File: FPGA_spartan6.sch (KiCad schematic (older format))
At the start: 46 parts, among them J6 Conn_02x10_Odd_Even, U10 lx9_XC6SLX9-TQ144, U11 FSM1LPTR, U12 FSM1LPTR, U13 FSM1LPTR, U9 CY7C199, X1 Oscillator_ASE-xxxMHz

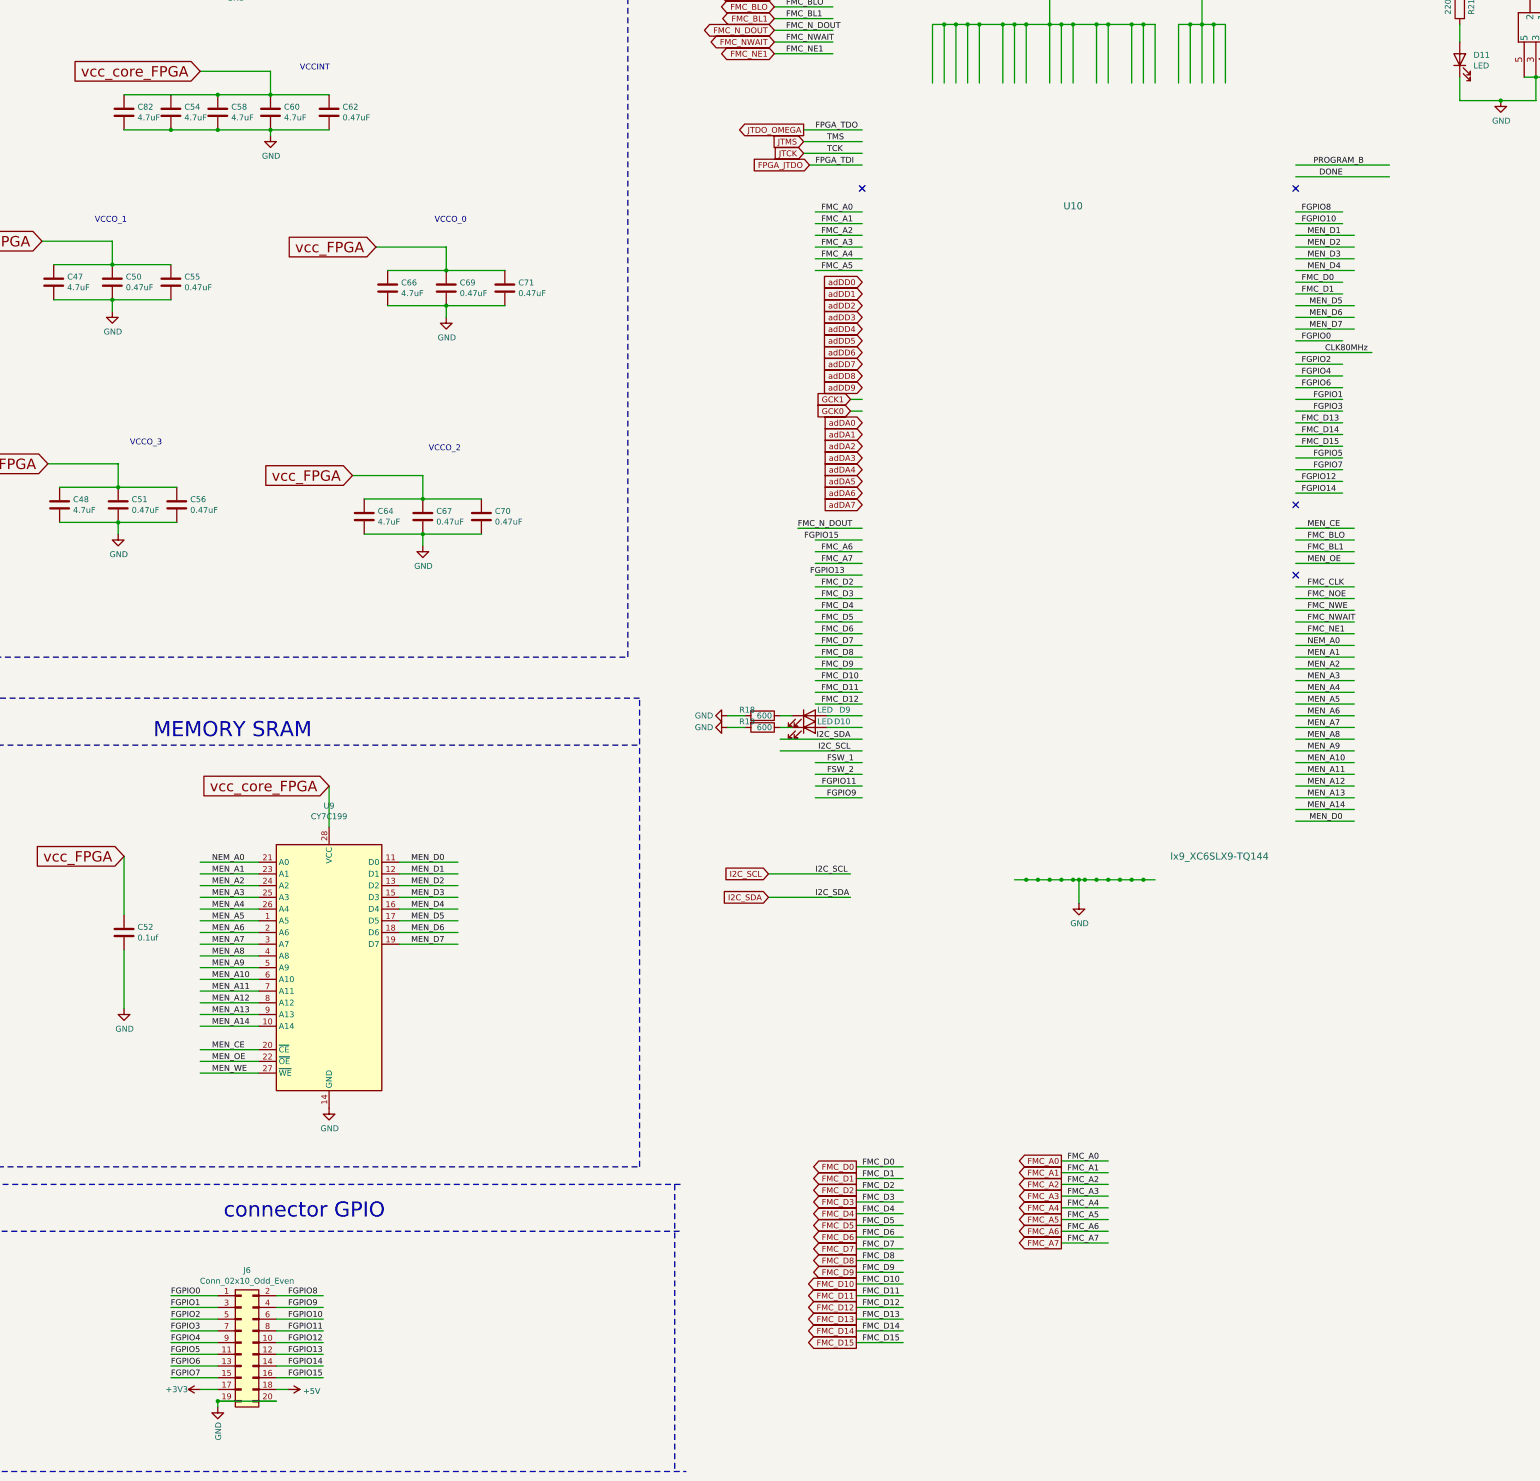
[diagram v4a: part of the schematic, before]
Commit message: diseño de esquematico fm
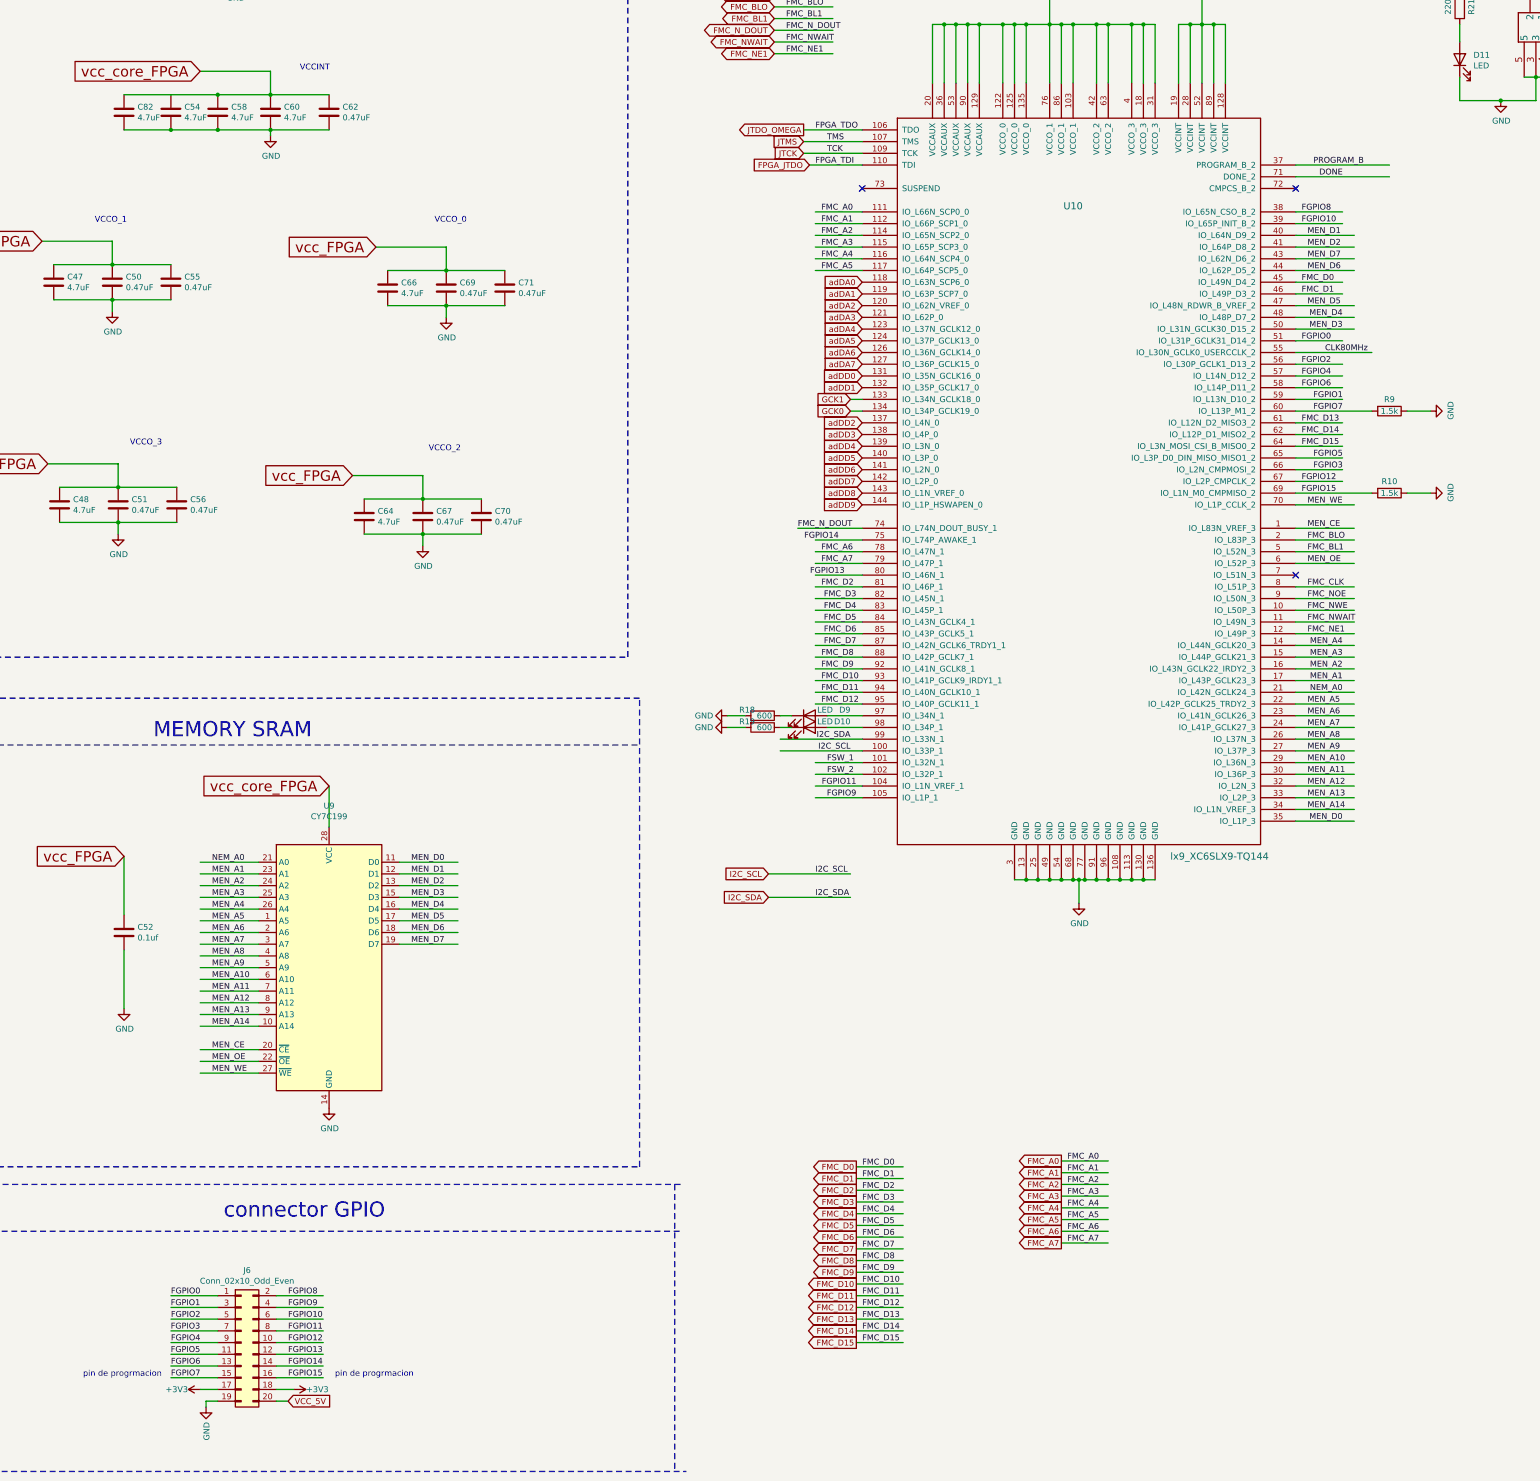
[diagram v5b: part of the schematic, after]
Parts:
- added R10, R9: 1.5k, Resistor_SMD:R_0603_1608Metric_Pad1.05x0.95mm_HandSolder, symbol BAT2032:R
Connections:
- net labels added: VCC_5V
- net labels removed: +5V
- wire segments 342 -> 346
- no-connect marks 4 -> 3
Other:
- note added: "pin de progrmacion\n"
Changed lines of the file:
@@
 	7700 13150 1200 13150
 Wire Wire Line
-	12950 5150 13450 5150
+	12950 5650 13450 5650
+Wire Wire Line
+	12950 5350 13450 5350
 Wire Wire Line
 	12950 5250 13450 5250
-Wire Wire Line
-	12950 5350 13450 5350
-Wire Wire Line
-	13450 5650 12950 5650
-Wire Wire Line
-	13450 5750 12950 5750
-Wire Wire Line
-	13450 5850 12950 5850
-Text Label 13050 5150 0    50   ~ 0
-MEN_D2
+Text Label 13050 5650 0    50   ~ 0
+MEN_D5
+Text Label 13050 5350 0    50   ~ 0
+MEN_D6
 Text Label 13050 5250 0    50   ~ 0
-MEN_D3
-Text Label 13050 5350 0    50   ~ 0
-MEN_D4
-Text Label 13350 5650 2    50   ~ 0
-MEN_D5
-Text Label 13350 5750 2    50   ~ 0
-MEN_D6
-Text Label 13350 5850 2    50   ~ 0
 MEN_D7
-Text Label 13050 5050 0    50   ~ 0
-MEN_D1
 Text Label 13350 10050 2    50   ~ 0
 MEN_D0
 Wire Wire Line
-	12950 5050 13450 5050
-Wire Wire Line
 	13450 10050 12950 10050
 Wire Wire Line
-	13450 8550 12950 8550
-Wire Wire Line
-	13450 8650 12950 8650
-Wire Wire Line
-	13450 8750 12950 8750
-Wire Wire Line
-	13450 8850 12950 8850
-Wire Wire Line
-	13450 8950 12950 8950
+	12950 8550 13450 8550
 Wire Wire Line
 	13450 9050 12950 9050
@@
 Wire Wire Line
 	13450 9950 12950 9950
-Text Label 13050 8550 0    50   ~ 0
-NEM_A0
-Text Label 13050 8650 0    50   ~ 0
-MEN_A1
-Text Label 13050 8750 0    50   ~ 0
-MEN_A2
-Text Label 13050 8850 0    50   ~ 0
-MEN_A3
 Text Label 13050 9050 0    50   ~ 0
 MEN_A5
-Text Label 13050 8950 0    50   ~ 0
+Text Label 13350 8550 2    50   ~ 0
 MEN_A4
 Text Label 13050 9150 0    50   ~ 0
@@
 	12950 5550 13350 5550
 Wire Wire Line
-	8850 8250 9250 8250
-Wire Wire Line
-	8850 8350 9250 8350
-Wire Wire Line
-	8850 8450 9250 8450
-Wire Wire Line
-	8850 8550 9250 8550
+	9250 8250 8850 8250
+Wire Wire Line
+	9250 8350 8850 8350
+Wire Wire Line
+	9250 8450 8850 8450
+Wire Wire Line
+	9250 8550 8850 8550
 Wire Wire Line
 	8850 8650 9250 8650
@@
 Text Label 13000 5550 0    50   ~ 0
 FMC_D1
-Text Label 8900 8250 0    50   ~ 0
+Text Label 9200 8250 2    50   ~ 0
 FMC_D4
-Text Label 8900 8350 0    50   ~ 0
+Text Label 9200 8350 2    50   ~ 0
 FMC_D5
-Text Label 8900 8450 0    50   ~ 0
+Text Label 9200 8450 2    50   ~ 0
 FMC_D6
-Text Label 8900 8550 0    50   ~ 0
+Text Label 9200 8550 2    50   ~ 0
 FMC_D7
 Text Label 8900 8650 0    50   ~ 0
@@
 Text Label 13000 6750 0    50   ~ 0
 FMC_D14
-Text Label 8900 8150 0    50   ~ 0
+Text Label 9200 8150 2    50   ~ 0
 FMC_D3
 Text Label 8900 8050 0    50   ~ 0
 FMC_D2
 Wire Wire Line
-	8850 8150 9250 8150
+	9250 8150 8850 8150
 Wire Wire Line
 	8850 8050 9250 8050
@@
 Text Label 13200 6050 0    50   ~ 0
 CLK80MHz
+Text GLabel 9250 7350 0    50   Input ~ 0
+adDD9
+Text GLabel 9250 7250 0    50   Input ~ 0
+adDD8
+Text GLabel 9250 7150 0    50   Input ~ 0
+adDD7
+Text GLabel 9250 7050 0    50   Input ~ 0
+adDD6
+Text GLabel 9250 6950 0    50   Input ~ 0
+adDD5
+Text GLabel 9250 6850 0    50   Input ~ 0
+adDD4
+Text GLabel 9250 6750 0    50   Input ~ 0
+adDD3
+Text GLabel 9250 6650 0    50   Input ~ 0
+adDD2
 Text GLabel 9250 6350 0    50   Input ~ 0
-adDD9
+adDD1
 Text GLabel 9250 6250 0    50   Input ~ 0
-adDD8
+adDD0
 Text GLabel 9250 6150 0    50   Input ~ 0
-adDD7
+adDA7
 Text GLabel 9250 6050 0    50   Input ~ 0
-adDD6
+adDA6
 Text GLabel 9250 5950 0    50   Input ~ 0
-adDD5
+adDA5
 Text GLabel 9250 5850 0    50   Input ~ 0
-adDD4
+adDA4
 Text GLabel 9250 5750 0    50   Input ~ 0
-adDD3
+adDA3
 Text GLabel 9250 5650 0    50   Input ~ 0
-adDD2
+adDA2
 Text GLabel 9250 5550 0    50   Input ~ 0
-adDD1
+adDA1
 Text GLabel 9250 5450 0    50   Input ~ 0
-adDD0
-Text GLabel 9250 7350 0    50   Input ~ 0
-adDA7
-Text GLabel 9250 7250 0    50   Input ~ 0
-adDA6
-Text GLabel 9250 7150 0    50   Input ~ 0
-adDA5
-Text GLabel 9250 7050 0    50   Input ~ 0
-adDA4
-Text GLabel 9250 6950 0    50   Input ~ 0
-adDA3
-Text GLabel 9250 6850 0    50   Input ~ 0
-adDA2
-Text GLabel 9250 6750 0    50   Input ~ 0
-adDA1
-Text GLabel 9250 6650 0    50   Input ~ 0
 adDA0
 $Comp
@@
 	12950 6450 13350 6450
 Wire Wire Line
-	12950 6550 13350 6550
-Wire Wire Line
 	12950 6950 13350 6950
 Wire Wire Line
@@
 FGPIO1
 Text Label 13100 6550 0    50   ~ 0
-FGPIO3
+FGPIO7
 Text Label 13100 6950 0    50   ~ 0
 FGPIO5
 Text Label 13100 7050 0    50   ~ 0
-FGPIO7
+FGPIO3
 Wire Wire Line
 	13350 4850 12950 4850
@@
 Wire Wire Line
 	13350 7150 12950 7150
-Wire Wire Line
-	13350 7250 12950 7250
 Text Label 13000 4850 0    50   ~ 0
 FGPIO8
@@
 FGPIO12
 Text Label 13000 7250 0    50   ~ 0
-FGPIO14
+FGPIO15
 Wire Wire Line
 	9250 9850 8850 9850
@@
 FGPIO13
 Text Label 9050 7650 2    50   ~ 0
-FGPIO15
-NoConn ~ 12950 7350
+FGPIO14
 NoConn ~ 9250 4650
 Wire Wire Line
@@
 $Comp
 L power-rescue:lx9_XC6SLX9-TQ144-pcb_edu-cache U10
-U 0 0 5CE650EB
+U 1 1 5CE650EB
 P 11150 7150
 F 0 "U10" H 11050 9500 60  0000 C CNN
@@
 F 3 "https://www.xilinx.com/support/documentation/data_sheets/ds162.pdf" H 11150 7150 50  0001 C CNN
 F 4 "122-1745-ND" H 11150 7150 50  0001 C CNN "digiker"
-	0    11150 7150
+	1    11150 7150
 	1    0    0    -1
 $EndComp
@@
 	1    0    0    -1
 $EndComp
-Wire Wire Line
-	4250 15000 3750 15000
 Text Label 3600 14200 2    50   ~ 0
 FGPIO1
@@
 L power:GND #PWR060
 U 1 1 5F8F6CEA
-P 3750 15050
-F 0 "#PWR060" H 3750 14800 50  0001 C CNN
-F 1 "GND" V 3755 14922 50  0000 R CNN
-F 2 "" H 3750 15050 50  0001 C CNN
-F 3 "" H 3750 15050 50  0001 C CNN
-	1    3750 15050
-	1    0    0    -1
-$EndComp
-Wire Wire Line
-	3750 15050 3750 15000
-Connection ~ 3750 15000
+P 3650 15050
+F 0 "#PWR060" H 3650 14800 50  0001 C CNN
+F 1 "GND" V 3655 14922 50  0000 R CNN
+F 2 "" H 3650 15050 50  0001 C CNN
+F 3 "" H 3650 15050 50  0001 C CNN
+	1    3650 15050
+	1    0    0    -1
+$EndComp
 Wire Wire Line
 	3600 14900 3750 14900
-$Comp
-L power:+5V #PWR063
-U 1 1 5F97EB1C
-P 4350 14900
-F 0 "#PWR063" H 4350 14750 50  0001 C CNN
-F 1 "+5V" V 4365 15028 50  0000 L CNN
-F 2 "" H 4350 14900 50  0001 C CNN
-F 3 "" H 4350 14900 50  0001 C CNN
-	1    4350 14900
-	0    1    1    0
-$EndComp
-Wire Wire Line
-	4350 14900 4250 14900
 Text GLabel 9150 6450 0    50   Input ~ 0
 GCK1
@@
 Wire Wire Line
 	3900 2850 3900 2800
+$Comp
+L BAT2032:R R?
+U 1 1 5D014E10
+P 13750 6550
+AR Path="/5D3DE78E/5D014E10" Ref="R?"  Part="1"
+AR Path="/5CF5B080/5D014E10" Ref="R9"  Part="1"
+F 0 "R9" V 13650 6550 50  0000 C CNN
+F 1 "1.5k" V 13750 6550 50  0000 C CNN
+F 2 "Resistor_SMD:R_0603_1608Metric_Pad1.05x0.95mm_HandSolder" V 13680 6550 50  0001 C CNN
+F 3 "~" H 13750 6550 50  0001 C CNN
+	1    13750 6550
+	0    1    1    0
+$EndComp
+$Comp
+L power:GND #PWR0146
+U 1 1 5D0A4D77
+P 14100 6550
+F 0 "#PWR0146" H 14100 6300 50  0001 C CNN
+F 1 "GND" H 14105 6377 50  0000 C CNN
+F 2 "" H 14100 6550 50  0001 C CNN
+F 3 "" H 14100 6550 50  0001 C CNN
+	1    14100 6550
+	0    -1   -1   0
+$EndComp
+Wire Wire Line
+	14100 6550 13900 6550
+Wire Wire Line
+	12950 6550 13600 6550
+$Comp
+L BAT2032:R R?
+U 1 1 5D1342FF
+P 13750 7250
+AR Path="/5D3DE78E/5D1342FF" Ref="R?"  Part="1"
+AR Path="/5CF5B080/5D1342FF" Ref="R10"  Part="1"
+F 0 "R10" V 13650 7250 50  0000 C CNN
+F 1 "1.5k" V 13750 7250 50  0000 C CNN
+F 2 "Resistor_SMD:R_0603_1608Metric_Pad1.05x0.95mm_HandSolder" V 13680 7250 50  0001 C CNN
+F 3 "~" H 13750 7250 50  0001 C CNN
+	1    13750 7250
+	0    1    1    0
+$EndComp
+$Comp
+L power:GND #PWR0147
+U 1 1 5D134305
+P 14100 7250
+F 0 "#PWR0147" H 14100 7000 50  0001 C CNN
+F 1 "GND" H 14105 7077 50  0000 C CNN
+F 2 "" H 14100 7250 50  0001 C CNN
+F 3 "" H 14100 7250 50  0001 C CNN
+	1    14100 7250
+	0    -1   -1   0
+$EndComp
+Wire Wire Line
+	14100 7250 13900 7250
+Wire Wire Line
+	12950 7250 13600 7250
+$Comp
+L power:+3V3 #PWR?
+U 1 1 5D22AF37
+P 4400 14900
+AR Path="/5CD17BDC/5D22AF37" Ref="#PWR?"  Part="1"
+AR Path="/5CF5B080/5D22AF37" Ref="#PWR0148"  Part="1"
+F 0 "#PWR0148" H 4400 14750 50  0001 C CNN
+F 1 "+3V3" V 4400 15100 50  0000 C CNN
+F 2 "" H 4400 14900 50  0001 C CNN
+F 3 "" H 4400 14900 50  0001 C CNN
+	1    4400 14900
+	0    1    1    0
+$EndComp
+Wire Wire Line
+	4400 14900 4250 14900
+Wire Wire Line
+	3650 15050 3650 15000
+Wire Wire Line
+	3650 15000 3750 15000
+Text GLabel 4350 15000 2    50   Input ~ 0
+VCC_5V
+Wire Wire Line
+	4350 15000 4250 15000
+Text Notes 4750 14800 0    50   ~ 0
+pin de progrmacion\n
+Text Notes 2600 14800 0    50   ~ 0
+pin de progrmacion\n
+Wire Wire Line
+	13450 7350 12950 7350
+Text Label 13050 7350 0    50   ~ 0
+MEN_WE
+Wire Wire Line
+	12950 5050 13450 5050
+Text Label 13050 5050 0    50   ~ 0
+MEN_D1
+Text Label 13350 5750 2    50   ~ 0
+MEN_D4
+Text Label 13350 5850 2    50   ~ 0
+MEN_D3
+Text Label 13050 5150 0    50   ~ 0
+MEN_D2
+Wire Wire Line
+	13450 5750 12950 5750
+Wire Wire Line
+	13450 5850 12950 5850
+Wire Wire Line
+	12950 5150 13450 5150
+Text Label 13350 8650 2    50   ~ 0
+MEN_A3
+Text Label 13350 8750 2    50   ~ 0
+MEN_A2
+Text Label 13350 8850 2    50   ~ 0
+MEN_A1
+Text Label 13350 8950 2    50   ~ 0
+NEM_A0
+Wire Wire Line
+	12950 8650 13450 8650
+Wire Wire Line
+	12950 8750 13450 8750
+Wire Wire Line
+	12950 8850 13450 8850
+Wire Wire Line
+	12950 8950 13450 8950
 $EndSCHEMATC

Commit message: diseño de esquematico CASI FINAL
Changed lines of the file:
@@
-EESchema Schematic File Version 4
+EESchema Schematic File Version 5
 LIBS:power-cache
 EELAYER 29 0
@@
 Text Label 13000 5950 0    50   ~ 0
 FGPIO0
+Text Label 8900 9850 0    50   ~ 0
+FGPIO6
+Wire Wire Line
+	12950 6450 13350 6450
+Wire Wire Line
+	12950 6950 13350 6950
+Wire Wire Line
+	12950 7050 13350 7050
 Text Label 13000 6150 0    50   ~ 0
-FGPIO2
-Text Label 13000 6250 0    50   ~ 0
-FGPIO4
-Text Label 13000 6350 0    50   ~ 0
-FGPIO6
-Wire Wire Line
-	12950 6450 13350 6450
-Wire Wire Line
-	12950 6950 13350 6950
-Wire Wire Line
-	12950 7050 13350 7050
-Text Label 13100 6450 0    50   ~ 0
 FGPIO1
 Text Label 13100 6550 0    50   ~ 0
 FGPIO7
-Text Label 13100 6950 0    50   ~ 0
-FGPIO5
-Text Label 13100 7050 0    50   ~ 0
-FGPIO3
 Wire Wire Line
 	13350 4850 12950 4850
@@
 Text Label 13000 4850 0    50   ~ 0
 FGPIO8
-Text Label 13000 4950 0    50   ~ 0
-FGPIO10
-Text Label 13000 7150 0    50   ~ 0
-FGPIO12
 Text Label 13000 7250 0    50   ~ 0
 FGPIO15
@@
 Wire Wire Line
 	9250 7650 8850 7650
-Text Label 9200 9850 2    50   ~ 0
+Text Label 13250 4950 2    50   ~ 0
 FGPIO9
-Text Label 9200 9750 2    50   ~ 0
+Text Label 13250 6450 2    50   ~ 0
 FGPIO11
-Text Label 9100 7950 2    50   ~ 0
-FGPIO13
-Text Label 9050 7650 2    50   ~ 0
-FGPIO14
 NoConn ~ 9250 4650
 Wire Wire Line
@@
 Wire Wire Line
 	12950 8950 13450 8950
+Text Label 9200 7650 2    50   ~ 0
+FGPIO13
+Text Label 9200 9750 2    50   ~ 0
+FGPIO14
+Text Label 8900 7950 0    50   ~ 0
+FGPIO5
+Text Label 13050 7150 0    50   ~ 0
+FGPIO4
+Text Label 13000 7050 0    50   ~ 0
+FGPIO12
+Text Label 13000 6950 0    50   ~ 0
+FGPIO3
+Text Label 13000 6350 0    50   ~ 0
+FGPIO2
+Text Label 13000 6250 0    50   ~ 0
+FGPIO10
 $EndSCHEMATC

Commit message: programacion luego del diseño del embebido
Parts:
- C52, C72: value 0.1uf -> 0.1uF
- R18, R19: value 600 -> 750
- R20, R21: value 220 -> 200
- U9: Digikey 428-2013-ND -> (none); digikey (none) -> 428-2013-ND
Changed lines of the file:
@@
 AR Path="/5CF5B080/5CECCD7A" Ref="C72"  Part="1"
 F 0 "C72" H 17415 3546 50  0000 L CNN
-F 1 "0.1uf" H 17415 3455 50  0000 L CNN
+F 1 "0.1uF" H 17415 3455 50  0000 L CNN
 F 2 "Capacitor_SMD:C_0603_1608Metric_Pad1.05x0.95mm_HandSolder" H 17338 3350 50  0001 C CNN
 F 3 "" H 17300 3500 50  0001 C CNN
@@
 F 2 "Package_SO:TSOP-I-28_11.8x8mm_P0.55mm" H 4700 11300 50  0001 C CNN
 F 3 "https://www.cypress.com/file/42731/download" H 4700 11300 50  0001 C CNN
-F 4 "428-2013-ND" H 4700 11300 50  0001 C CNN "Digikey"
+F 4 "428-2013-ND" H 4700 11300 50  0001 C CNN "digikey"
 	1    4700 11300
 	1    0    0    -1
@@
 AR Path="/5CF5B080/5CF20F0E" Ref="C52"  Part="1"
 F 0 "C52" H 3065 11046 50  0000 L CNN
-F 1 "0.1uf" H 3065 10955 50  0000 L CNN
+F 1 "0.1uF" H 3065 10955 50  0000 L CNN
 F 2 "Capacitor_SMD:C_0603_1608Metric_Pad1.05x0.95mm_HandSolder" H 2988 10850 50  0001 C CNN
 F 3 "" H 2950 11000 50  0001 C CNN
@@
 AR Path="/5CF5B080/5D2D175A" Ref="R20"  Part="1"
 F 0 "R20" V 14250 2500 50  0000 C CNN
-F 1 "220" V 14450 2500 50  0000 C CNN
+F 1 "200" V 14450 2500 50  0000 C CNN
 F 2 "Resistor_SMD:R_0603_1608Metric_Pad1.05x0.95mm_HandSolder" V 14280 2500 50  0001 C CNN
 F 3 "~" H 14350 2500 50  0001 C CNN
@@
 AR Path="/5CF5B080/5D313D9F" Ref="R21"  Part="1"
 F 0 "R21" V 14250 3100 50  0000 C CNN
-F 1 "220" V 14450 3100 50  0000 C CNN
+F 1 "200" V 14450 3100 50  0000 C CNN
 F 2 "Resistor_SMD:R_0603_1608Metric_Pad1.05x0.95mm_HandSolder" V 14280 3100 50  0001 C CNN
 F 3 "~" H 14350 3100 50  0001 C CNN
@@
 AR Path="/5CF5B080/5DA7B6B8" Ref="R18"  Part="1"
 F 0 "R18" V 8350 8950 50  0000 L CNN
-F 1 "600" V 8400 9100 50  0000 L CNN
+F 1 "750" V 8400 9100 50  0000 L CNN
 F 2 "Resistor_SMD:R_0603_1608Metric_Pad1.05x0.95mm_HandSolder" V 8330 9150 50  0001 C CNN
 F 3 "~" H 8400 9150 50  0001 C CNN
-F 4 "" H 8400 9150 50  0001 C CNN "Digikey"
 	1    8400 9150
 	0    1    1    0
@@
 AR Path="/5CF5B080/5E0AAA8E" Ref="R19"  Part="1"
 F 0 "R19" V 8350 9050 50  0000 L CNN
-F 1 "600" V 8400 9200 50  0000 L CNN
+F 1 "750" V 8400 9200 50  0000 L CNN
 F 2 "Resistor_SMD:R_0603_1608Metric_Pad1.05x0.95mm_HandSolder" V 8330 9250 50  0001 C CNN
 F 3 "~" H 8400 9250 50  0001 C CNN
-F 4 "" H 8400 9250 50  0001 C CNN "Digikey"
 	1    8400 9250
 	0    1    1    0
